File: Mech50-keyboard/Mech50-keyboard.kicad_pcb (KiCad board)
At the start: 2 copper layers, 256 x 96 mm, 196 parts, among them U1 Elite-C

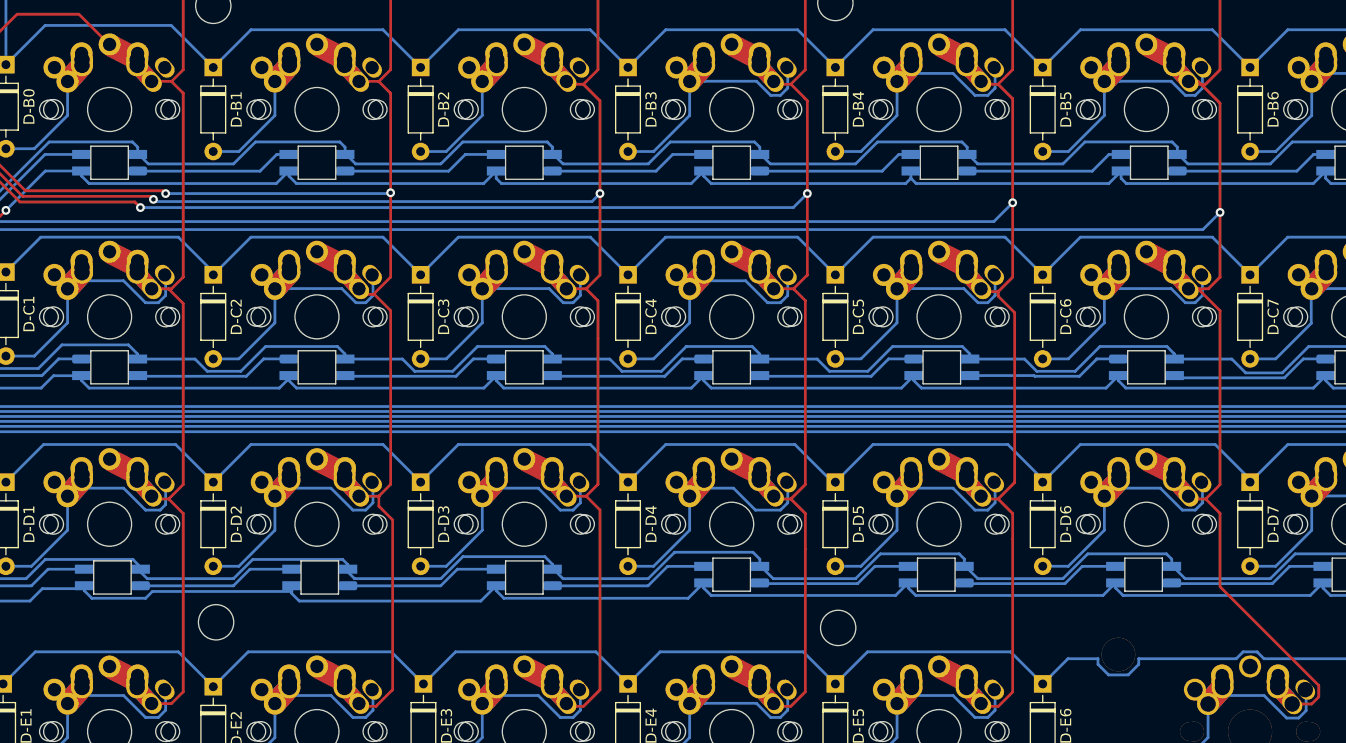
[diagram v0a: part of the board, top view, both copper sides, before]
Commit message: fixed some bugs with low profile switches
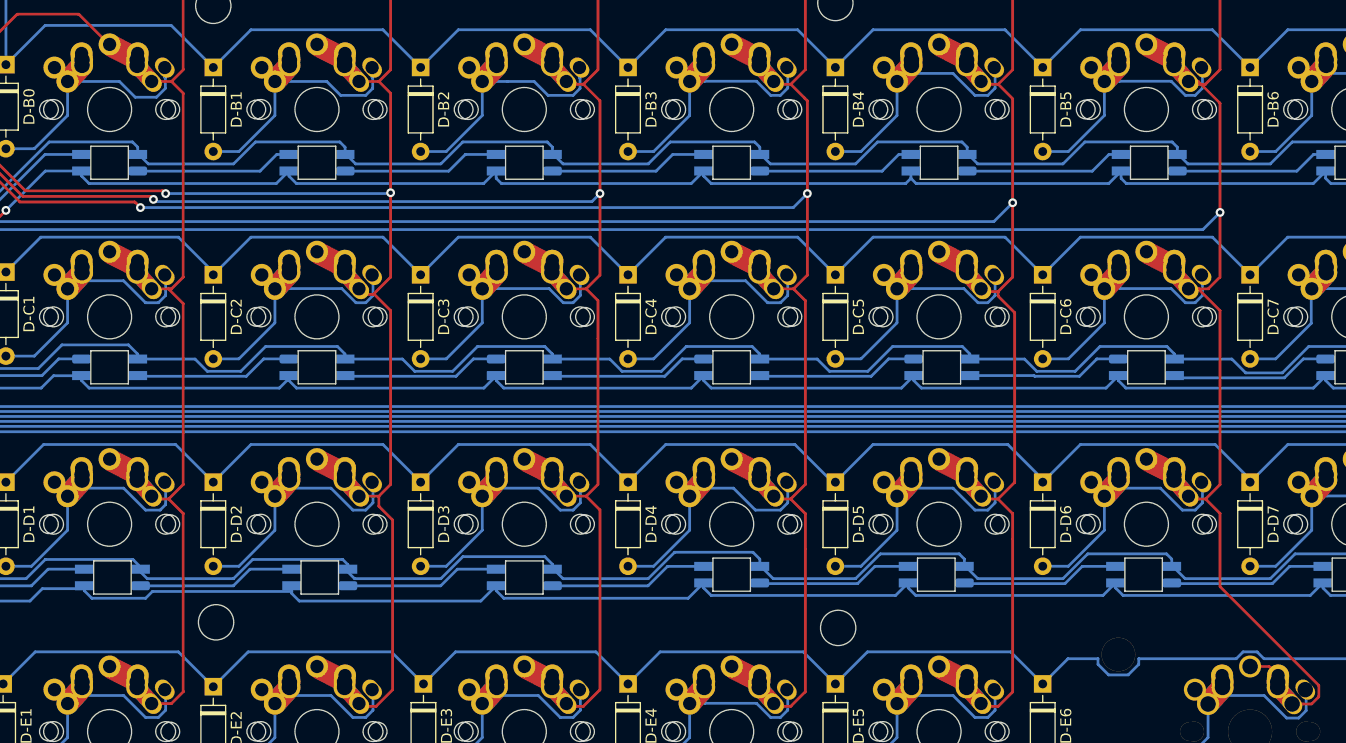
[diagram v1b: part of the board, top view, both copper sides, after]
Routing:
- net Net-(D-B0-Pad2): track 9.92 -> 21.6 mm
- net Net-(D-B2-Pad2): track 10.0 -> 21.6 mm
- net Net-(D-A1-Pad2): track 74.0 -> 85.5 mm
- net Net-(S-A5-Pad2): track 242.5 -> 245.4 mm
